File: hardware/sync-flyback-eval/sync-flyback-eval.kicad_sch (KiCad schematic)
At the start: 78 parts, among them J1 RJ45_LED_Shielded, Q1 SiR422DP, Q2 Si7898DP, Q3 MMDT3906, T1 PoE_Transformer, T2 Pulse_Transformer, U1 TPS23754PWPR, U2 TCMT1107

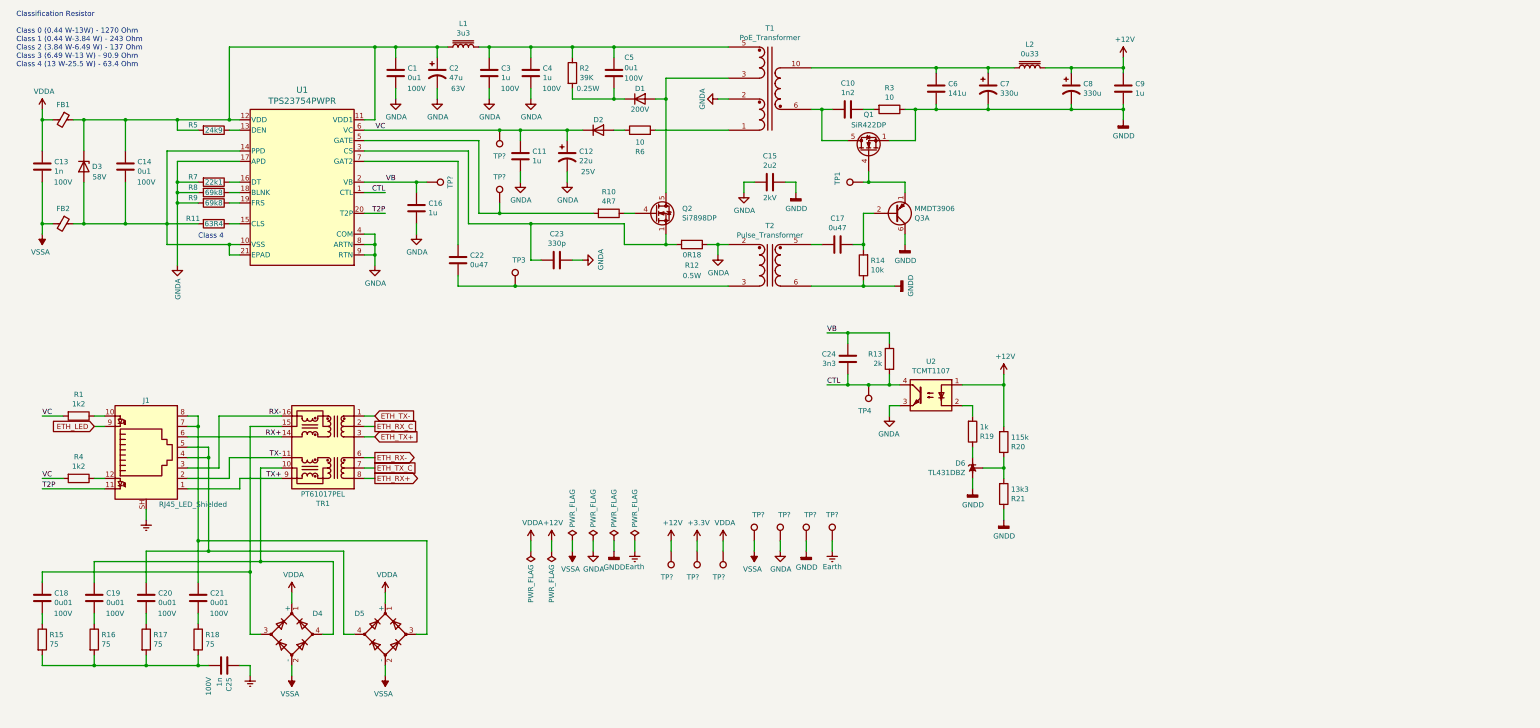
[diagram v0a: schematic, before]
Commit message: flyback: various fixes
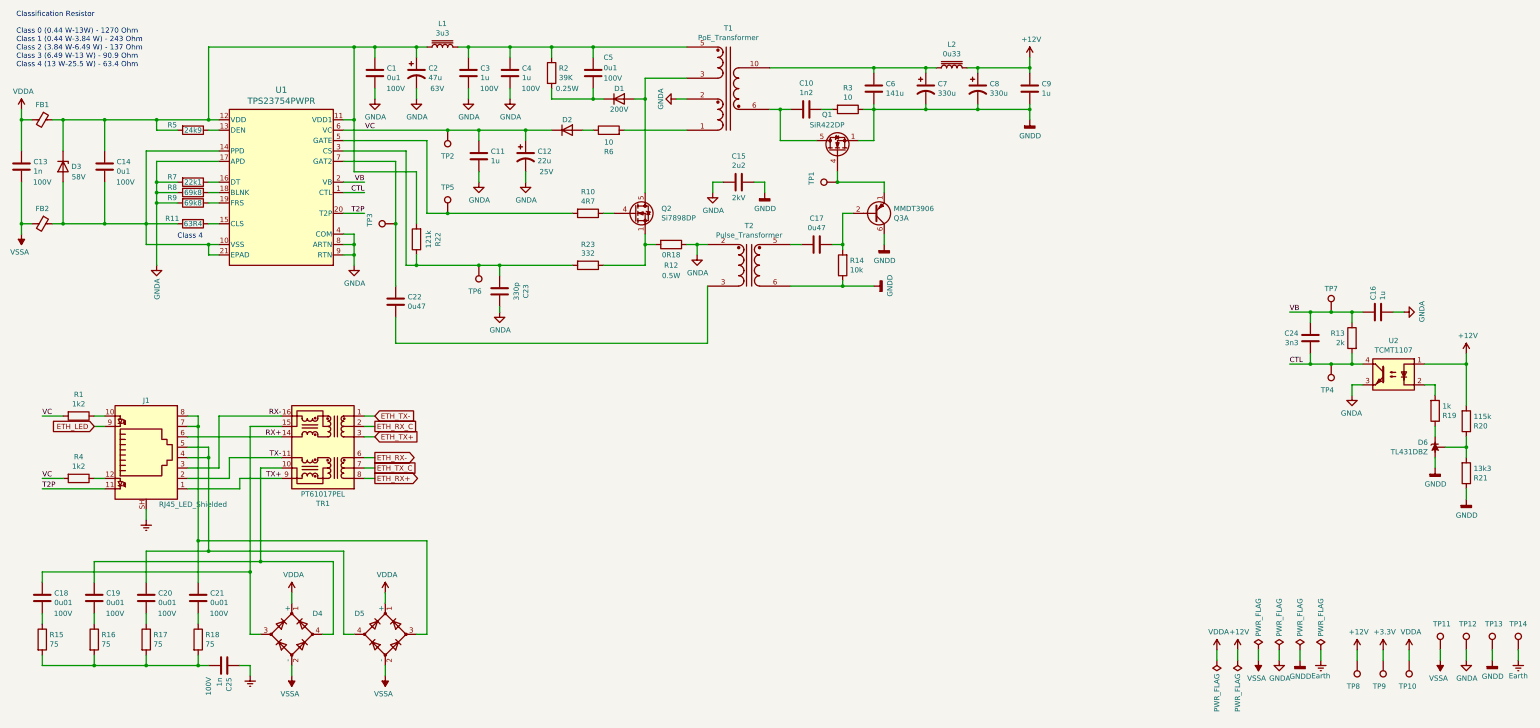
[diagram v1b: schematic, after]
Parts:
- removed TP?: VB, TestPoint:TestPoint_Pad_1.5x1.5mm, symbol Connector:TestPoint
- added R22: 121k, Resistor_SMD:R_0402_1005Metric, symbol Device:R
- added R23: 332, Resistor_SMD:R_0402_1005Metric, symbol Device:R
- added TP6: CS, TestPoint:TestPoint_Pad_1.5x1.5mm, symbol Connector:TestPoint
- added TP7: VB, TestPoint:TestPoint_Pad_1.5x1.5mm, symbol Connector:TestPoint
- TP3: value TestPoint -> GAT2
- gave numbers to parts that had none: 9
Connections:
- net VB: now also TP7.1
- net at C1.1, C14.1, C2.1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: now also R22.2
- net at Q2.1 (S), Q2.2 (S), Q2.3 (S)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: now also R23.1; no longer C23.2, U1.3 (CS)
- net at C22.1, T2.3 (AB): no longer TP3.1
- net at C22.2, U1.7 (GAT2): now also TP3.1
- new net: C23.2, R22.1, R23.2, TP6.1, U1.3 (CS)
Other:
- moved on the sheet: C1, C10, C11, C12, C13, C14, C15, C17, C2, C22, C23, C24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

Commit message: flyback: use trimpots for tunable inputs
DT (gate-to-gate dead time), FRS (switching frequency), and
BLNK (blanking period).
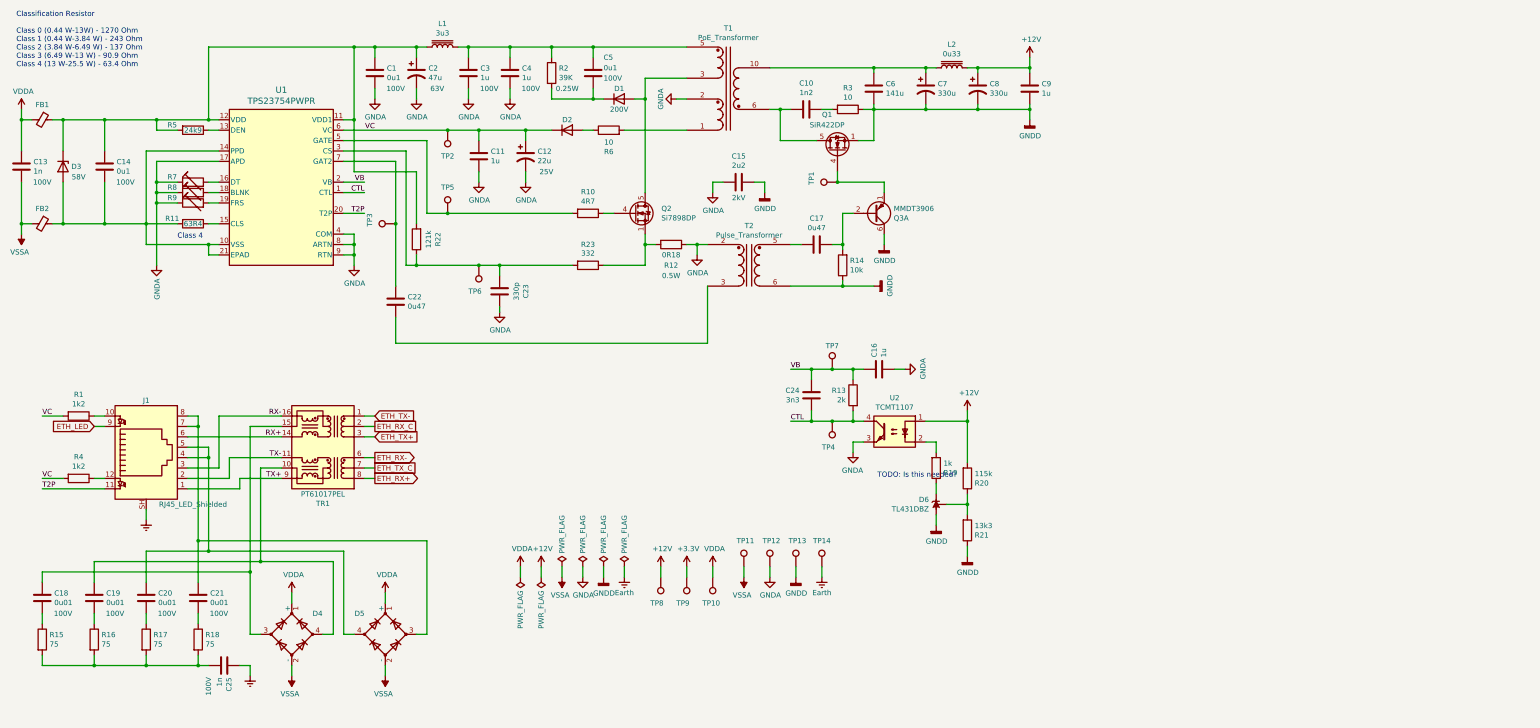
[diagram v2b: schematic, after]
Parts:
- removed R7: 22k1, Resistor_SMD:R_0402_1005Metric, symbol Device:R
- removed R8, R9: 69k8, Resistor_SMD:R_0402_1005Metric, symbol Device:R
- added R7, R8, R9: R_Trim, symbol Device:R_Trim
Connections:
- net GNDA: now also R7.1, R8.1, R9.1
- net at U1.16 (DT): now also R7.2
- net at U1.18 (BLNK): now also R8.2
- net at U1.19 (FRS): now also R9.2
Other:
- note added: "TODO: Is this needed?"
- moved on the sheet: C16, C24, D6, R13, R19, R20, R21, TP10, TP11, TP12, TP13, TP14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

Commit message: flyback: fix converter bypass capacitor value
This is the capacitor between the high and low sides of the
converter. It is specified as 2200 pF, which I misconverted to 2.2 uF
instead of 2.2 nF.
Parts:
- C15: value 2u2 -> 2n2
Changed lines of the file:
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@@
     (in_bom yes) (on_board yes)
     (property "Reference" "C15" (id 0) (at 190.5 50.8 90))
-    (property "Value" "2u2" (id 1) (at 190.5 53.0606 90))
+    (property "Value" "2n2" (id 1) (at 190.5 53.0606 90))
     (property "Footprint" "Capacitor_SMD:C_0402_1005Metric" (id 2) (at 186.69 58.1152 0)
       (effects (font (size 1.27 1.27)) hide)
@@
     )
     (path "/00000000-0000-0000-0000-00005c50ea6b"
-      (reference "C15") (unit 1) (value "2u2") (footprint "Capacitor_SMD:C_0402_1005Metric")
+      (reference "C15") (unit 1) (value "2n2") (footprint "Capacitor_SMD:C_0402_1005Metric")
     )
     (path "/121ad5d1-d98c-400b-a918-25f7012138ea"

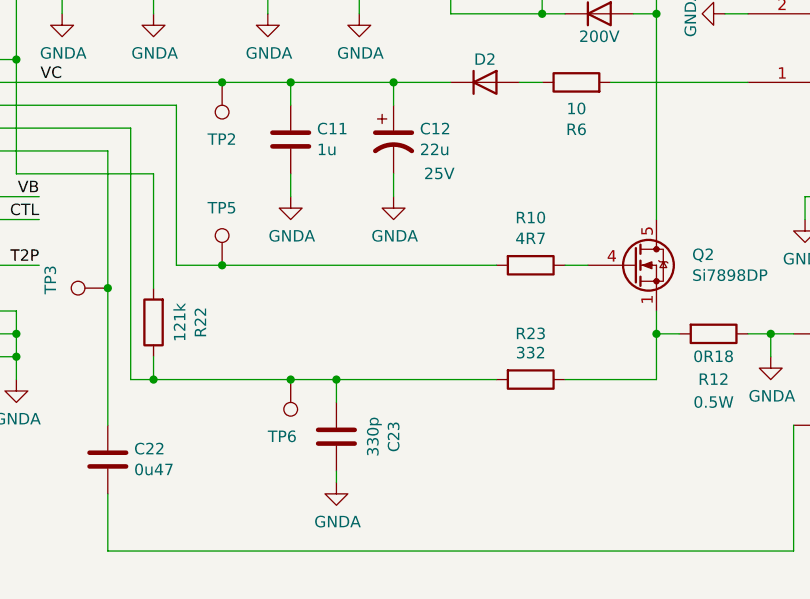
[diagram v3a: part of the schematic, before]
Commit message: flyback: add protection diode to gate
This was noted in the application note to have been added after the
initial design. It's purpose is unclear.
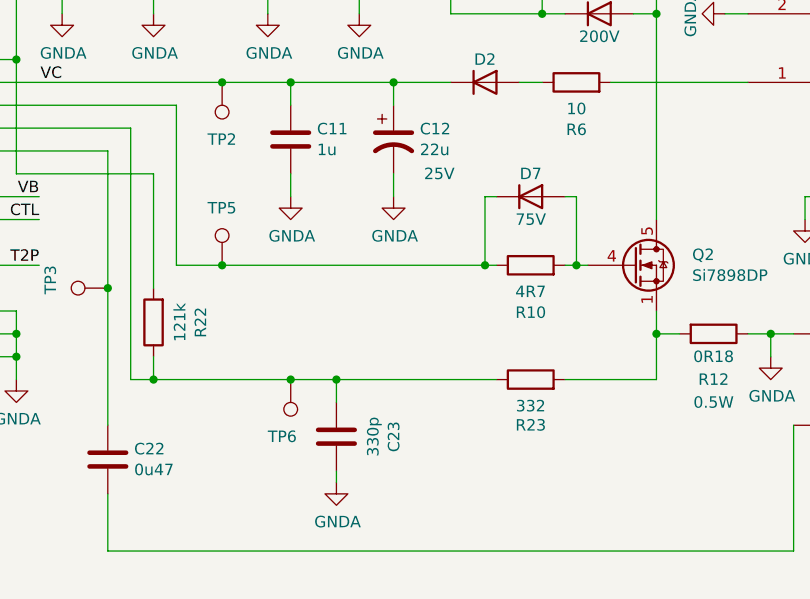
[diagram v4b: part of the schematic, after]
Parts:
- added D7: D, Diode_SMD:D_SOD-323, symbol Device:D
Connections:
- net at R10.1: now also TP5.1, U1.5 (GATE), D7.1 (K); no longer Q2.4 (G)
- net at Q2.1 (S), Q2.2 (S), Q2.3 (S)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: now also R23.2; no longer R23.1
- net at C23.2, R22.1, TP6.1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: now also R23.1; no longer R23.2
- new net: D7.2 (A), Q2.4 (G), R10.2
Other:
- moved on the sheet: R10, R23
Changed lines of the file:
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@@
   (junction (at 134.62 24.13) (diameter 0) (color 0 0 0 0)
   )
+  (junction (at 148.59 64.77) (diameter 0) (color 0 0 0 0)
+  )
+  (junction (at 158.75 64.77) (diameter 0) (color 0 0 0 0)
+  )
   (junction (at 119.38 64.77) (diameter 0) (color 0 0 0 0)
   )
@@
     (stroke (width 0) (type default) (color 0 0 0 0))
   )
+  (wire (pts (xy 149.86 57.15) (xy 148.59 57.15))
+    (stroke (width 0) (type default) (color 0 0 0 0))
+  )
   (wire (pts (xy 114.3 46.99) (xy 93.98 46.99))
     (stroke (width 0) (type default) (color 0 0 0 0))
@@
     (stroke (width 0) (type default) (color 0 0 0 0))
   )
+  (wire (pts (xy 148.59 64.77) (xy 149.86 64.77))
+    (stroke (width 0) (type default) (color 0 0 0 0))
+  )
   (wire (pts (xy 25.4 49.53) (xy 25.4 41.91))
     (stroke (width 0) (type default) (color 0 0 0 0))
@@
     (stroke (width 0) (type default) (color 0 0 0 0))
   )
-  (wire (pts (xy 119.38 64.77) (xy 149.86 64.77))
+  (wire (pts (xy 119.38 64.77) (xy 148.59 64.77))
     (stroke (width 0) (type default) (color 0 0 0 0))
   )
@@
     (stroke (width 0) (type default) (color 0 0 0 0))
   )
-  (wire (pts (xy 157.48 64.77) (xy 160.02 64.77))
+  (wire (pts (xy 157.48 64.77) (xy 158.75 64.77))
     (stroke (width 0) (type default) (color 0 0 0 0))
   )
@@
     (stroke (width 0) (type default) (color 0 0 0 0))
   )
+  (wire (pts (xy 158.75 64.77) (xy 158.75 57.15))
+    (stroke (width 0) (type default) (color 0 0 0 0))
+  )
   (wire (pts (xy 162.56 44.45) (xy 177.8 44.45))
     (stroke (width 0) (type default) (color 0 0 0 0))
@@
     (stroke (width 0) (type default) (color 0 0 0 0))
   )
+  (wire (pts (xy 158.75 57.15) (xy 157.48 57.15))
+    (stroke (width 0) (type default) (color 0 0 0 0))
+  )
   (wire (pts (xy 48.26 41.91) (xy 60.96 41.91))
     (stroke (width 0) (type default) (color 0 0 0 0))
@@
     (stroke (width 0) (type default) (color 0 0 0 0))
   )
+  (wire (pts (xy 158.75 64.77) (xy 160.02 64.77))
+    (stroke (width 0) (type default) (color 0 0 0 0))
+  )
   (wire (pts (xy 138.43 46.99) (xy 138.43 44.45))
     (stroke (width 0) (type default) (color 0 0 0 0))
@@
     (stroke (width 0) (type default) (color 0 0 0 0))
   )
+  (wire (pts (xy 148.59 57.15) (xy 148.59 64.77))
+    (stroke (width 0) (type default) (color 0 0 0 0))
+  )
   (wire (pts (xy 71.12 167.64) (xy 71.12 152.4))
     (stroke (width 0) (type default) (color 0 0 0 0))
@@
     (pin "2")
   )
-  (symbol (lib_id "Device:R") (at 153.67 64.77 270) (unit 1)
+  (symbol (lib_id "Device:R") (at 153.67 64.77 90) (unit 1)
     (in_bom yes) (on_board yes)
-    (property "Reference" "R10" (id 0) (at 153.67 59.5122 90))
-    (property "Value" "4R7" (id 1) (at 153.67 61.8236 90))
-    (property "Footprint" "Resistor_SMD:R_0402_1005Metric" (id 2) (at 153.67 62.992 90)
+    (property "Reference" "R10" (id 0) (at 153.67 70.0278 90))
+    (property "Value" "4R7" (id 1) (at 153.67 67.7164 90))
+    (property "Footprint" "Resistor_SMD:R_0402_1005Metric" (id 2) (at 153.67 66.548 90)
       (effects (font (size 1.27 1.27)) hide)
     )
@@
     (pin "1")
   )
+  (symbol (lib_id "Device:D") (at 153.67 57.15 0) (unit 1)
+    (in_bom yes) (on_board yes)
+    (property "Reference" "D7" (id 0) (at 153.67 54.61 0))
+    (property "Value" "D" (id 1) (at 153.67 53.975 0)
+      (effects (font (size 1.27 1.27)) hide)
+    )
+    (property "Footprint" "Diode_SMD:D_SOD-323" (id 2) (at 153.67 57.15 0)
+      (effects (font (size 1.27 1.27)) hide)
+    )
+    (property "Datasheet" "~" (id 3) (at 153.67 57.15 0)
+      (effects (font (size 1.27 1.27)) hide)
+    )
+    (property "Voltage" "75V" (id 4) (at 153.67 59.69 0))
+    (pin "1")
+    (pin "2")
+  )
   (symbol (lib_id "Device:C") (at 224.79 102.87 90) (unit 1)
     (in_bom yes) (on_board yes)
@@
     (pin "1")
   )
-  (symbol (lib_id "Device:R") (at 153.67 77.47 270) (unit 1)
+  (symbol (lib_id "Device:R") (at 153.67 77.47 90) (unit 1)
     (in_bom yes) (on_board yes)
-    (property "Reference" "R23" (id 0) (at 153.67 72.39 90))
-    (property "Value" "332" (id 1) (at 153.67 74.5236 90))
-    (property "Footprint" "Resistor_SMD:R_0402_1005Metric" (id 2) (at 153.67 75.692 90)
+    (property "Reference" "R23" (id 0) (at 153.67 82.55 90))
+    (property "Value" "332" (id 1) (at 153.67 80.4164 90))
+    (property "Footprint" "Resistor_SMD:R_0402_1005Metric" (id 2) (at 153.67 79.248 90)
       (effects (font (size 1.27 1.27)) hide)
     )
@@
       (reference "D6") (unit 1) (value "TL431DBZ") (footprint "Package_TO_SOT_SMD:SOT-23")
     )
+    (path "/10642cdc-17a5-4001-ba2a-ab8283d8ec44"
+      (reference "D7") (unit 1) (value "D") (footprint "Diode_SMD:D_SOD-323")
+    )
     (path "/00000000-0000-0000-0000-00005d56eab6"
